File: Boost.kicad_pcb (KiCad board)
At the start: 2 copper layers, 68.6 x 40.1 mm, 17 parts, among them J1 Conn_01x03, J2 Conn_01x02, Q1 IRF740, U1 MAX1771ESA

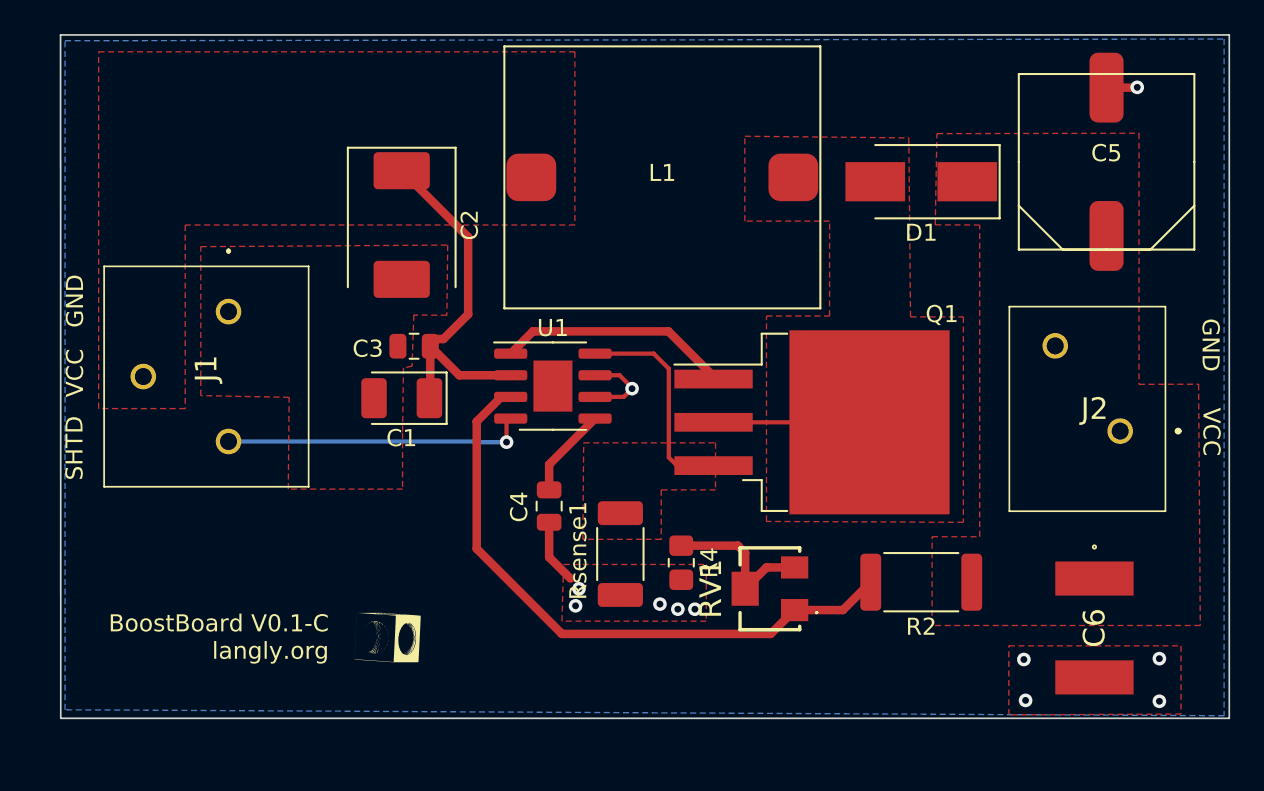
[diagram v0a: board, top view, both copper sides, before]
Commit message: Added version v0.1-D
- Moved stuff much closer
- Increased the width of the traces
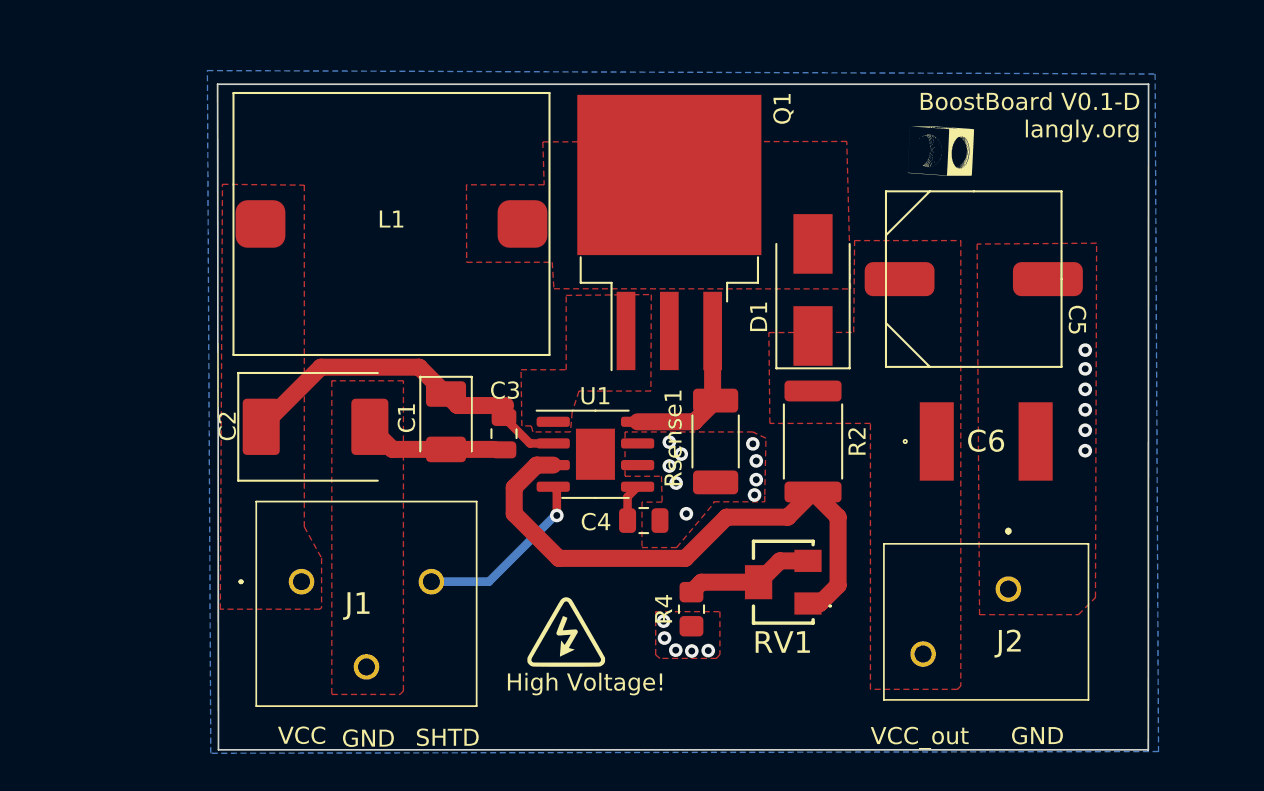
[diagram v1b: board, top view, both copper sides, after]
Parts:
- added G***: LOGO, LOGO, F.Cu at (111.3, 72.1)
- moved G*** 43.2 mm to (133.2, 43.9)
- moved J1 16.4 mm to (95.7, 69.2), turned to 180 degrees
- moved L1 16.1 mm to (101.0, 48.2)
- moved Q1 13.9 mm to (117.3, 48.7), turned to 90 degrees
- moved C2 12.9 mm to (96.5, 60.1), turned to 0 degrees
- moved C6 12.6 mm to (135.9, 61.0), turned to 0 degrees
- moved J2 11.4 mm to (137.2, 69.6), turned to 90 degrees
- moved R2 10.4 mm to (125.7, 61.0), turned to -90 degrees
- moved C5 10.4 mm to (135.2, 51.4), turned to -90 degrees
- moved D1 8.98 mm to (125.7, 52.1), turned to 90 degrees
- moved Rsense1 8.65 mm to (120.0, 61.0)
- moved C3 7.36 mm to (107.6, 60.5), turned to -90 degrees
- moved C4 5.61 mm to (115.8, 65.6), turned to 0 degrees
- moved U1 4.71 mm to (113.0, 61.7)
- moved C1 2.94 mm to (104.2, 59.8), turned to -90 degrees
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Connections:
- net Net-(D1-A) renamed /I_OUT
- net Net-(Q1-G) renamed toggle
- J1 pad 1: /GND -> /VCC
- J1 pad 2: /VCC -> /GND
- J2 pad 1: /VCC_OUT -> /GND
- J2 pad 2: /GND -> /VCC_OUT
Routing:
- net toggle: track 13.7 -> 0.00 mm
- net /I_OUT: track 9.20 -> 0.00 mm
- net Net-(J1-Pin_3): track 17.8 -> 10.7 mm
- net FB: track 36.5 -> 32.9 mm
- net CS: track 12.7 -> 9.25 mm
- net Net-(U1-REF): track 5.30 -> 2.23 mm
- net /GND: track 10.5 -> 7.84 mm, vias 11 -> 20
- net Net-(R4-Pad1): track 9.45 -> 7.60 mm
- net /VCC: track 21.5 -> 20.2 mm
- added copper zone on F.Cu, net toggle
- removed copper zone on F.Cu, net CS
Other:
- board size 68.6 x 40.1 mm -> 54.6 x 39 mm
- board text added: "BoostBoard V0.1-D langly.org"
- board text added: "High Voltage!"
- board text added: "VCC_out"
- board text removed: "BoostBoard V0.1-C langly.org"

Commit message: Working on revision 0.1-E
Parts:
- removed the G*** at (111.3, 72.1)
- moved G*** 19.1 mm to (114.2, 43.8)
- moved R4 15.8 mm to (133.5, 76.0), turned to 0 degrees
- moved C6 15.3 mm to (141.0, 46.5), turned to 90 degrees
- moved Q1 11.4 mm to (116.6, 60.1)
- moved D1 10.6 mm to (115.9, 48.2), turned to 180 degrees
- moved U1 10.4 mm to (114.4, 72.0)
- moved J2 9.92 mm to (137.5, 59.7), turned to 180 degrees
- moved C4 8.14 mm to (119.6, 72.8), turned to 90 degrees
- moved C3 6.52 mm to (109.1, 66.8), turned to 0 degrees
- moved Rsense1 6.47 mm to (125.1, 65.0), turned to 90 degrees
- moved C5 6.08 mm to (131.0, 47.0), turned to 0 degrees
- moved RV1 5.94 mm to (127.5, 74.0), turned to 0 degrees
- moved R2 5.74 mm to (130.2, 64.6)
- moved C1 2.90 mm to (106.7, 61.3), turned to 180 degrees
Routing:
- net /GND: track 7.84 -> 30.6 mm, vias 20 -> 12
- net /VCC: track 20.2 -> 33.1 mm
- net CS: track 9.25 -> 0.00 mm
- net Net-(U1-REF): track 2.23 -> 2.83 mm
- added copper zone on F.Cu, net CS
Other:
- board text added: "BoostBoard V0.1-E langly.org"
- board text removed: "BoostBoard V0.1-D langly.org"
- board text removed: "High Voltage!"
- board text removed: "VCC_out"
